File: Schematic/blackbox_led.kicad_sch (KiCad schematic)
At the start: 26 parts, among them U10 CSNP1GCR01-BOW

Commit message: Refactor code structure for improved readability and maintainability
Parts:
- removed U10: CSNP1GCR01-BOW, fch7_fp:CSNP1GCR01-BOW, symbol fclib:CSNP1GCR01-BOW
- added U6: CSNP1GCR01-BOW, fch7_fp:CSNP1GCR01-BOW, symbol fclib:CSNP1GCR01-BOW
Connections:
- net GND: now also U6.4 (VSS)
- net SDIO_CLK: now also U6.3 (SCLK)
- net SDIO_CMD: now also U6.8 (CMD)
- net SDIO_D0: now also U6.7 (SDD0)
- net SDIO_D1: now also U6.6 (SDD1)
- net SDIO_D2: now also U6.1 (SDD2)
- net SDIO_D3: now also U6.2 (CD/SDD3)
- net VDD_MCU: now also U6.5 (VCC)
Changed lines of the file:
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@@
 		(on_board yes)
 		(dnp no)
-		(property "Reference" "U10"
-			(at 207.264 85.09 0)
+		(fields_autoplaced yes)
+		(property "Reference" "U6"
+			(at 206.375 83.82 0)
 			(effects
 				(font
@@
 		)
 		(property "Value" "CSNP1GCR01-BOW"
-			(at 207.264 87.63 0)
+			(at 206.375 86.36 0)
 			(effects
 				(font
@@
 			)
 		)
-		(pin "5"
+		(pin "4"
+		)
+		(pin "3"
+		)
+		(pin "2"
+		)
+		(pin "6"
+		)
+		(pin "7"
 		)
 		(pin "1"
 		)
-		(pin "2"
-		)
-		(pin "4"
-		)
-		(pin "7"
-		)
-		(pin "3"
-		)
 		(pin "8"
 		)
-		(pin "6"
+		(pin "5"
 		)
 		(instances
 			(project ""
 				(path "/11716af6-0e6e-444b-b738-3f12da23c1a2/fc7fa8bf-8ca0-46b3-82d5-3a5223b4ca6b"
-					(reference "U10")
+					(reference "U6")
 					(unit 1)
 				)

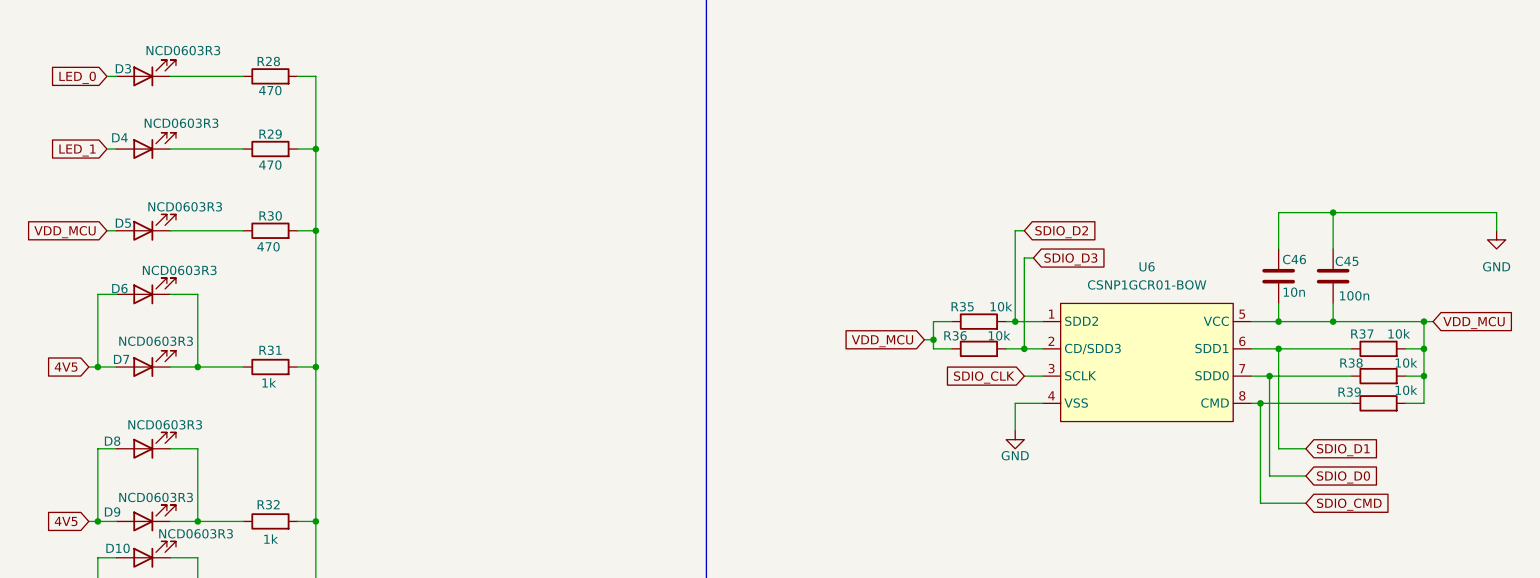
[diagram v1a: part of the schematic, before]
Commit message: Refactor schematic files and add net definitions
- Updated priority values for GND and POWER net classes in fch7.kicad_pro.
- Added USB_DIFF net class with associated patterns for USB differential signals.
- Removed duplicate junctions and adjusted wire connections in rf_rx.kicad_sch for clarity.
- Adjusted component positions and properties in rf_rx.kicad_sch for better layout.
- Modified text positions for IMU components in sensors.kicad_sch to improve readability.
- Cleaned up unnecessary wires and added new connections in sensors.kicad_sch.
- Introduced nets.txt file to define various electrical nets used across the schematics.
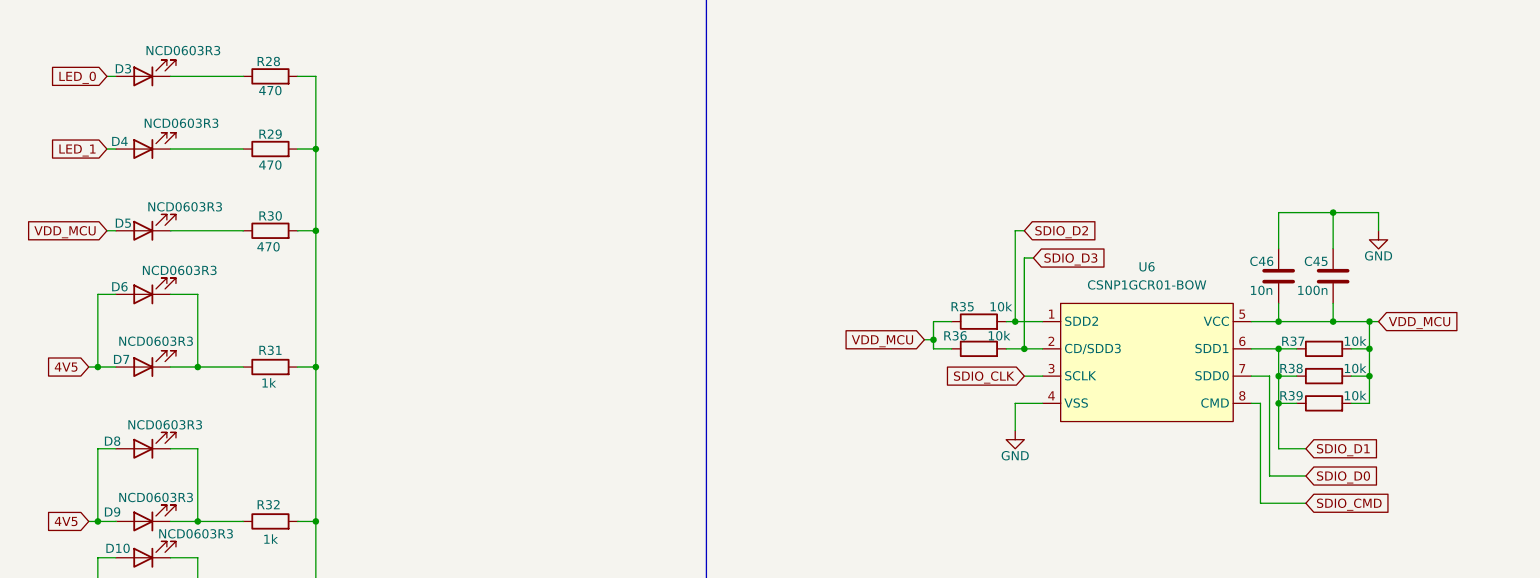
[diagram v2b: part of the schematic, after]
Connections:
- net SDIO_CMD: no longer R39.1
- net SDIO_D0: no longer R38.1
- net SDIO_D1: now also R38.1, R39.1
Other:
- moved on the sheet: R37, R38, R39

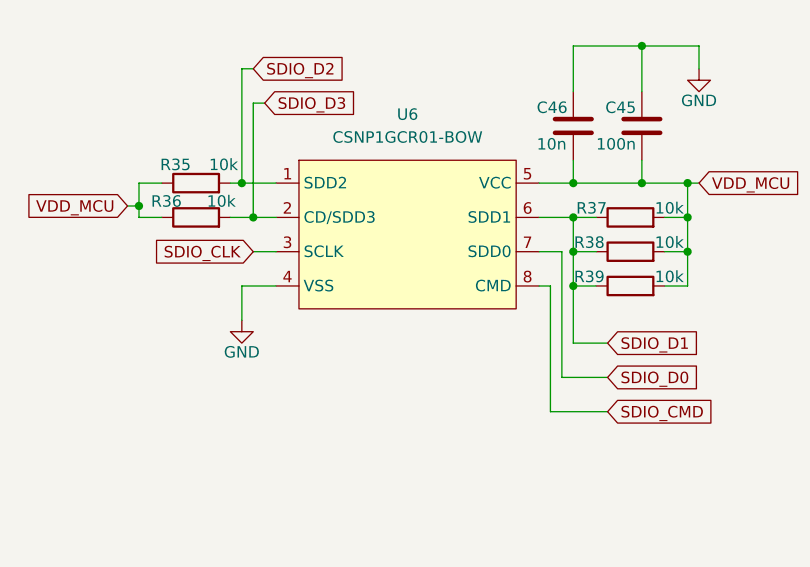
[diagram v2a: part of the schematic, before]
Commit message: Update global label for SDIO and modify wire connections in blackbox LED schematic
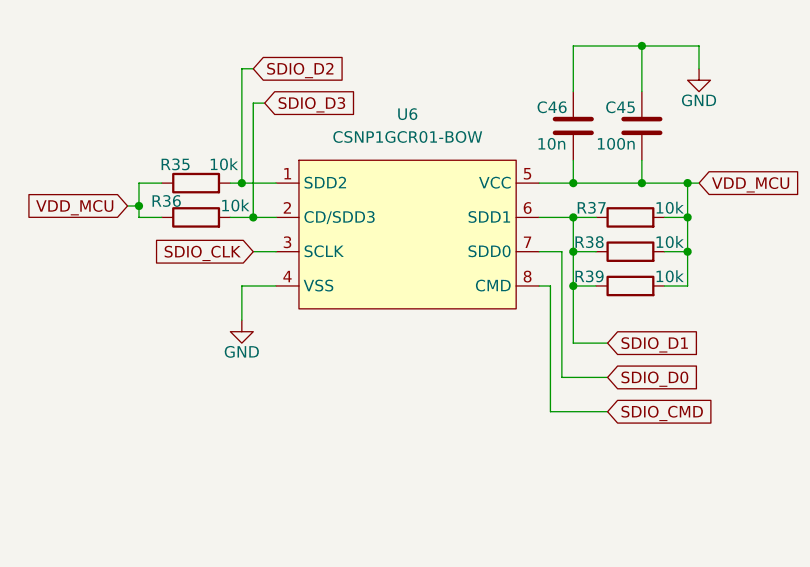
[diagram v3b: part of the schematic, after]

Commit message: Re-introduced MPU6500, every component in place with their 3d model, every track is routed
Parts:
- D10, D11, D12, D13, D3, D4, D5, D6, D7, D8, D9: footprint fch7_fp:LED0603-R-RD_RED -> LED_SMD:LED_0603_1608Metric
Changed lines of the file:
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@@
 			)
 		)
-		(property "Footprint" "fch7_fp:LED0603-R-RD_RED"
+		(property "Footprint" "LED_SMD:LED_0603_1608Metric"
 			(at 66.04 119.38 0)
 			(effects
@@
 			)
 		)
-		(property "Footprint" "fch7_fp:LED0603-R-RD_RED"
+		(property "Footprint" "LED_SMD:LED_0603_1608Metric"
 			(at 64.77 144.78 0)
 			(effects
@@
 			)
 		)
-		(property "Footprint" "fch7_fp:LED0603-R-RD_RED"
+		(property "Footprint" "LED_SMD:LED_0603_1608Metric"
 			(at 66.04 97.79 0)
 			(effects
@@
 			)
 		)
-		(property "Footprint" "fch7_fp:LED0603-R-RD_RED"
+		(property "Footprint" "LED_SMD:LED_0603_1608Metric"
 			(at 66.04 57.15 0)
 			(effects
@@
 			)
 		)
-		(property "Footprint" "fch7_fp:LED0603-R-RD_RED"
+		(property "Footprint" "LED_SMD:LED_0603_1608Metric"
 			(at 66.04 78.74 0)
 			(effects
@@
 			)
 		)
-		(property "Footprint" "fch7_fp:LED0603-R-RD_RED"
+		(property "Footprint" "LED_SMD:LED_0603_1608Metric"
 			(at 66.04 87.63 0)
 			(effects
@@
 			)
 		)
-		(property "Footprint" "fch7_fp:LED0603-R-RD_RED"
+		(property "Footprint" "LED_SMD:LED_0603_1608Metric"
 			(at 66.04 67.31 0)
 			(effects
@@
 			)
 		)
-		(property "Footprint" "fch7_fp:LED0603-R-RD_RED"
+		(property "Footprint" "LED_SMD:LED_0603_1608Metric"
 			(at 66.04 109.22 0)
 			(effects
@@
 			)
 		)
-		(property "Footprint" "fch7_fp:LED0603-R-RD_RED"
+		(property "Footprint" "LED_SMD:LED_0603_1608Metric"
 			(at 66.04 134.62 0)
 			(effects
@@
 			)
 		)
-		(property "Footprint" "fch7_fp:LED0603-R-RD_RED"
+		(property "Footprint" "LED_SMD:LED_0603_1608Metric"
 			(at 64.77 154.94 0)
 			(effects
@@
 			)
 		)
-		(property "Footprint" "fch7_fp:LED0603-R-RD_RED"
+		(property "Footprint" "LED_SMD:LED_0603_1608Metric"
 			(at 66.04 124.46 0)
 			(effects

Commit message: finished every routing and fix errors in DRC
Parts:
- U6: footprint fch7_fp:CSNP1GCR01-BOW -> fch7:CSNP1GCR01-BOW
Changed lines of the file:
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@@
 			)
 		)
-		(property "Footprint" "fch7_fp:CSNP1GCR01-BOW"
+		(property "Footprint" "fch7:CSNP1GCR01-BOW"
 			(at 207.01 96.52 0)
 			(effects

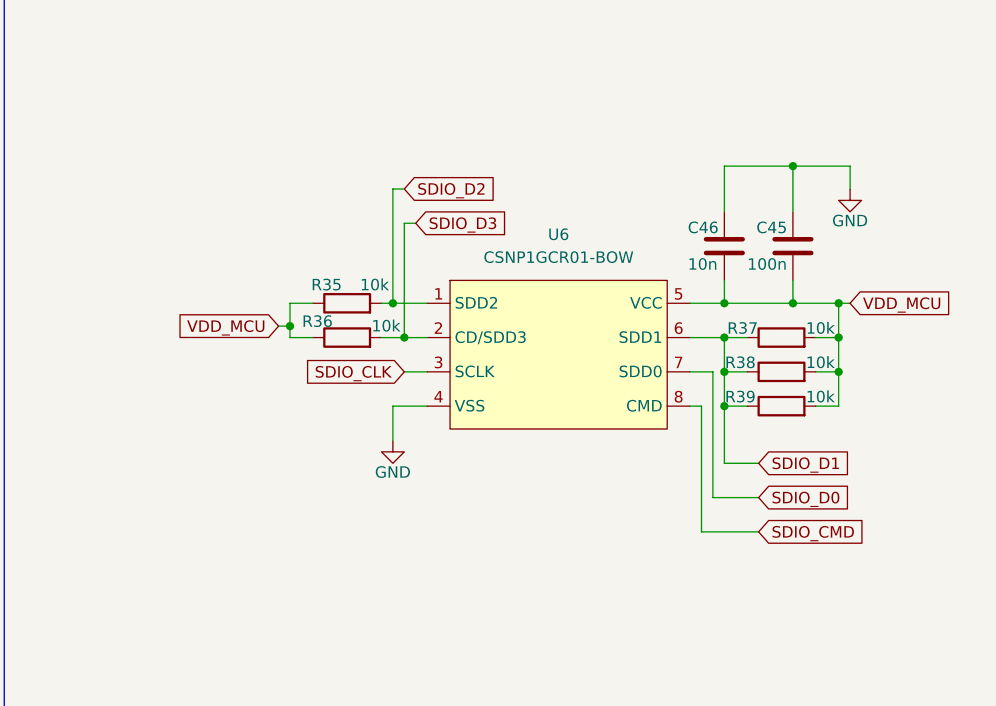
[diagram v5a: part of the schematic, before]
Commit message: update schematic after reviewing some footprints
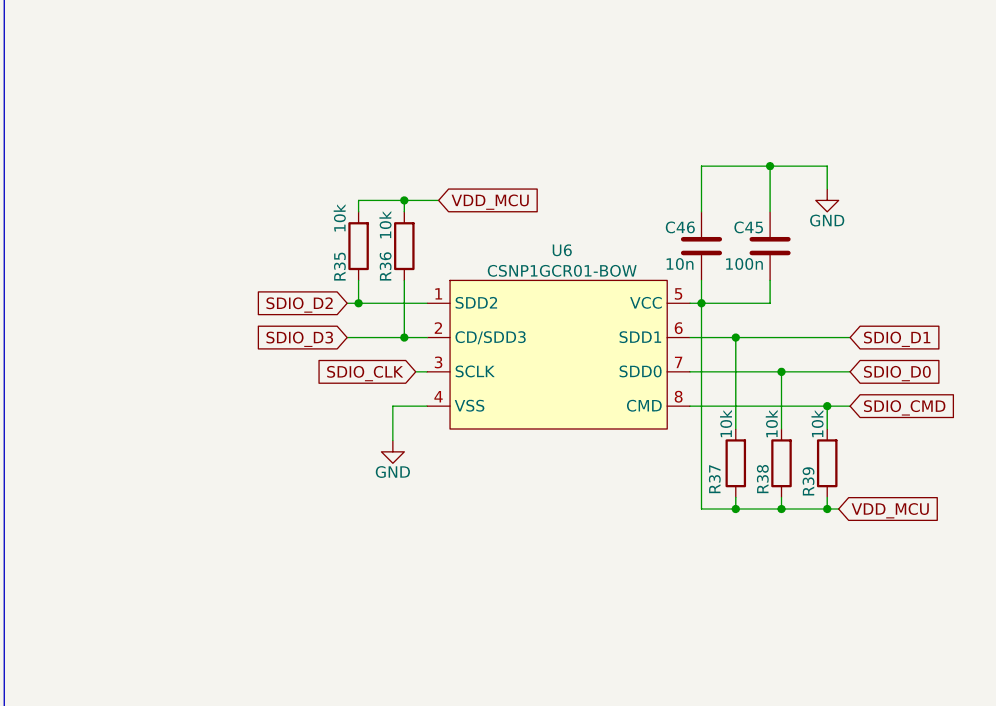
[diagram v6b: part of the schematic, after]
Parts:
- C45: MPN 0603B104K500NT -> (none); Manufacturer FH -> (none)
- C46: MPN CC0603KRX7R9BB103 -> (none); Manufacturer YAGEO -> (none)
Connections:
- net SDIO_CMD: now also R39.2
- net SDIO_D0: now also R38.2
- net SDIO_D1: now also R37.2; no longer R37.1, R38.1, R39.1
- net SDIO_D2: now also R35.1; no longer R35.2
- net SDIO_D3: now also R36.1; no longer R36.2
- net VDD_MCU: now also R35.2, R36.2, R37.1, R38.1, R39.1; no longer R35.1, R36.1, R37.2, R38.2, R39.2
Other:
- moved on the sheet: C45, C46, R35, R36, R37, R38, R39

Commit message: minor update
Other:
- note added: "1Gbit/128MO SDNAND flash memory for blackbox storage"
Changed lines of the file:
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@@
+		)
+	)
+	(text "1Gbit/128MO SDNAND flash memory for blackbox storage"
+		(exclude_from_sim no)
+		(at 220.726 47.752 0)
+		(effects
+			(font
+				(size 1.27 1.27)
+			)
 		)
 	)
@@
 		(on_board yes)
 		(dnp no)
-		(fields_autoplaced yes)
 		(property "Reference" "#PWR038"
 			(at 90.17 162.56 0)
@@
 		)
 		(property "Value" "GND"
-			(at 90.17 161.29 0)
+			(at 90.17 159.766 0)
 			(effects
 				(font
@@
 		)
 		(property "Value" "470"
-			(at 83.82 59.182 90)
-			(effects
-				(font
+			(at 83.82 59.69 90)
+			(effects
+				(font

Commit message: minor update and some checking
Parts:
- C45: MPN (none) -> C0603X5R1E104K030BB; Manufacturer (none) -> TDK
- C46: MPN (none) -> TMK063B7103KP-F; Manufacturer (none) -> TAIYO YUDEN
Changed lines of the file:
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@@
 			)
 		)
-		(property "Datasheet" ""
+		(property "Datasheet" "https://product.tdk.com/system/files/dam/doc/product/capacitor/ceramic/mlcc/catalog/mlcc_commercial_general_en.pdf?ref_disty=mouser"
 			(at 229.87 85.09 0)
 			(effects
@@
 			)
 		)
-		(property "MPN" ""
+		(property "MPN" "C0603X5R1E104K030BB"
 			(at 229.87 85.09 0)
 			(effects
@@
 			)
 		)
-		(property "Manufacturer" ""
+		(property "Manufacturer" "TDK"
 			(at 229.87 85.09 0)
 			(effects
@@
 			)
 		)
-		(property "Datasheet" ""
+		(property "Datasheet" "https://www.yuden.co.jp/productdata/catalog/mlcc02_e.pdf"
 			(at 222.25 85.09 0)
 			(effects
@@
 			)
 		)
-		(property "MPN" ""
+		(property "MPN" "TMK063B7103KP-F "
 			(at 222.25 85.09 0)
 			(effects
@@
 			)
 		)
-		(property "Manufacturer" ""
+		(property "Manufacturer" "TAIYO YUDEN"
 			(at 222.25 85.09 0)
 			(effects
